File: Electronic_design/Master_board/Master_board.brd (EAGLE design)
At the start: 100 x 80 mm, 36 parts, among them IC1 74LS241N

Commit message: CRC OK
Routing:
- net VCC: track 99.8 -> 101.5 mm
- net VIN: track 51.7 -> 52.5 mm
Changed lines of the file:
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@@
 <wire x1="64.77" y1="76.2" x2="66.04" y2="76.2" width="0.508" layer="16"/>
 <wire x1="66.04" y1="76.2" x2="68.58" y2="73.66" width="0.508" layer="16"/>
-<wire x1="68.58" y1="73.66" x2="78.74" y2="73.66" width="0.508" layer="16"/>
-<wire x1="83.82" y1="78.74" x2="86.52920625" y2="78.74" width="0.508" layer="16"/>
-<wire x1="86.52920625" y1="78.74" x2="86.55460625" y2="78.7654" width="0.508" layer="16"/>
-<wire x1="95.18239375" y1="78.7654" x2="95.20779375" y2="78.74" width="0.508" layer="16"/>
-<wire x1="95.20779375" y1="78.74" x2="99.06" y2="78.74" width="0.508" layer="16"/>
-<wire x1="86.55460625" y1="78.7654" x2="95.18239375" y2="78.7654" width="0.508" layer="16"/>
-<wire x1="99.06" y1="78.74" x2="99.06" y2="71.12" width="0.508" layer="16"/>
+<wire x1="68.58" y1="73.66" x2="78.359" y2="73.66" width="0.508" layer="16"/>
+<wire x1="83.439" y1="78.994" x2="86.52920625" y2="78.994" width="0.508" layer="16"/>
+<wire x1="86.52920625" y1="78.994" x2="86.42760625" y2="79.0194" width="0.508" layer="16"/>
+<wire x1="95.56339375" y1="79.1464" x2="95.08079375" y2="79.121" width="0.508" layer="16"/>
+<wire x1="95.08079375" y1="79.121" x2="99.06" y2="79.121" width="0.508" layer="16"/>
+<wire x1="86.42760625" y1="79.0194" x2="95.56339375" y2="79.1464" width="0.508" layer="16"/>
+<wire x1="99.06" y1="79.121" x2="99.06" y2="71.12" width="0.508" layer="16"/>
 <wire x1="99.06" y1="71.12" x2="97.7618" y2="71.12" width="0.508" layer="16"/>
 <via x="97.7618" y="71.12" extent="1-16" drill="0.35"/>
-<wire x1="78.74" y1="73.66" x2="83.82" y2="78.74" width="0.508" layer="16"/>
+<wire x1="78.359" y1="73.66" x2="83.439" y2="78.994" width="0.508" layer="16"/>
 <wire x1="97.7618" y1="71.12" x2="96.4726625" y2="71.12" width="0.508" layer="1"/>
 </signal>
@@
 <wire x1="59.69" y1="76.2" x2="59.69" y2="72.39" width="2.54" layer="16"/>
 <wire x1="59.69" y1="72.39" x2="60.96" y2="71.12" width="2.54" layer="16"/>
-<wire x1="84.709" y1="77.089" x2="94.488" y2="77.089" width="2.54" layer="16"/>
-<wire x1="94.488" y1="77.089" x2="95.25" y2="76.327" width="2.54" layer="16"/>
+<wire x1="84.709" y1="77.216" x2="94.488" y2="77.216" width="2.54" layer="16"/>
+<wire x1="94.488" y1="77.216" x2="95.25" y2="76.327" width="2.54" layer="16"/>
 <wire x1="95.25" y1="76.327" x2="95.25" y2="73.66" width="2.54" layer="16"/>
 <wire x1="81.28" y1="71.12" x2="60.96" y2="71.12" width="2.54" layer="16"/>
-<wire x1="81.28" y1="71.12" x2="84.709" y2="77.089" width="2.54" layer="16"/>
+<wire x1="81.28" y1="71.12" x2="84.709" y2="77.216" width="2.54" layer="16"/>
 <wire x1="95.25" y1="73.66" x2="95.25" y2="67.31" width="2.54" layer="16"/>
 <contactref element="C3" pad="+"/>
@@
 <wire x1="15.24" y1="72.39" x2="16.51" y2="71.12" width="2.54" layer="1"/>
 <contactref element="C4" pad="+"/>
-<wire x1="16.51" y1="71.12" x2="15.748" y2="71.12" width="0" layer="19" extent="1-1"/>
+<wire x1="15.748" y1="71.12" x2="16.51" y2="71.12" width="0.1524" layer="1"/>
 </signal>
 <signal name="3V3">

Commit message: modif piste
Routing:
- net VCC: track 101.5 -> 100.5 mm
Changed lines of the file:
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@@
 <wire x1="66.04" y1="76.2" x2="68.58" y2="73.66" width="0.508" layer="16"/>
 <wire x1="68.58" y1="73.66" x2="78.359" y2="73.66" width="0.508" layer="16"/>
-<wire x1="83.439" y1="78.994" x2="86.52920625" y2="78.994" width="0.508" layer="16"/>
-<wire x1="86.52920625" y1="78.994" x2="86.42760625" y2="79.0194" width="0.508" layer="16"/>
-<wire x1="95.56339375" y1="79.1464" x2="95.08079375" y2="79.121" width="0.508" layer="16"/>
-<wire x1="95.08079375" y1="79.121" x2="99.06" y2="79.121" width="0.508" layer="16"/>
-<wire x1="86.42760625" y1="79.0194" x2="95.56339375" y2="79.1464" width="0.508" layer="16"/>
 <wire x1="99.06" y1="79.121" x2="99.06" y2="71.12" width="0.508" layer="16"/>
 <wire x1="99.06" y1="71.12" x2="97.7618" y2="71.12" width="0.508" layer="16"/>
 <via x="97.7618" y="71.12" extent="1-16" drill="0.35"/>
-<wire x1="78.359" y1="73.66" x2="83.439" y2="78.994" width="0.508" layer="16"/>
+<wire x1="78.359" y1="73.66" x2="83.42574375" y2="79.10675" width="0.508" layer="16"/>
+<wire x1="83.42574375" y1="79.10675" x2="83.439" y2="79.121" width="0.508" layer="16"/>
 <wire x1="97.7618" y1="71.12" x2="96.4726625" y2="71.12" width="0.508" layer="1"/>
+<wire x1="99.04575" y1="79.10675" x2="99.06" y2="79.121" width="0.508" layer="16"/>
+<wire x1="83.42574375" y1="79.10675" x2="99.04575" y2="79.10675" width="0.508" layer="16"/>
+<wire x1="99.04575" y1="79.10675" x2="99.06" y2="79.121" width="0.508" layer="16"/>
 </signal>
 <signal name="CTRL_AX">

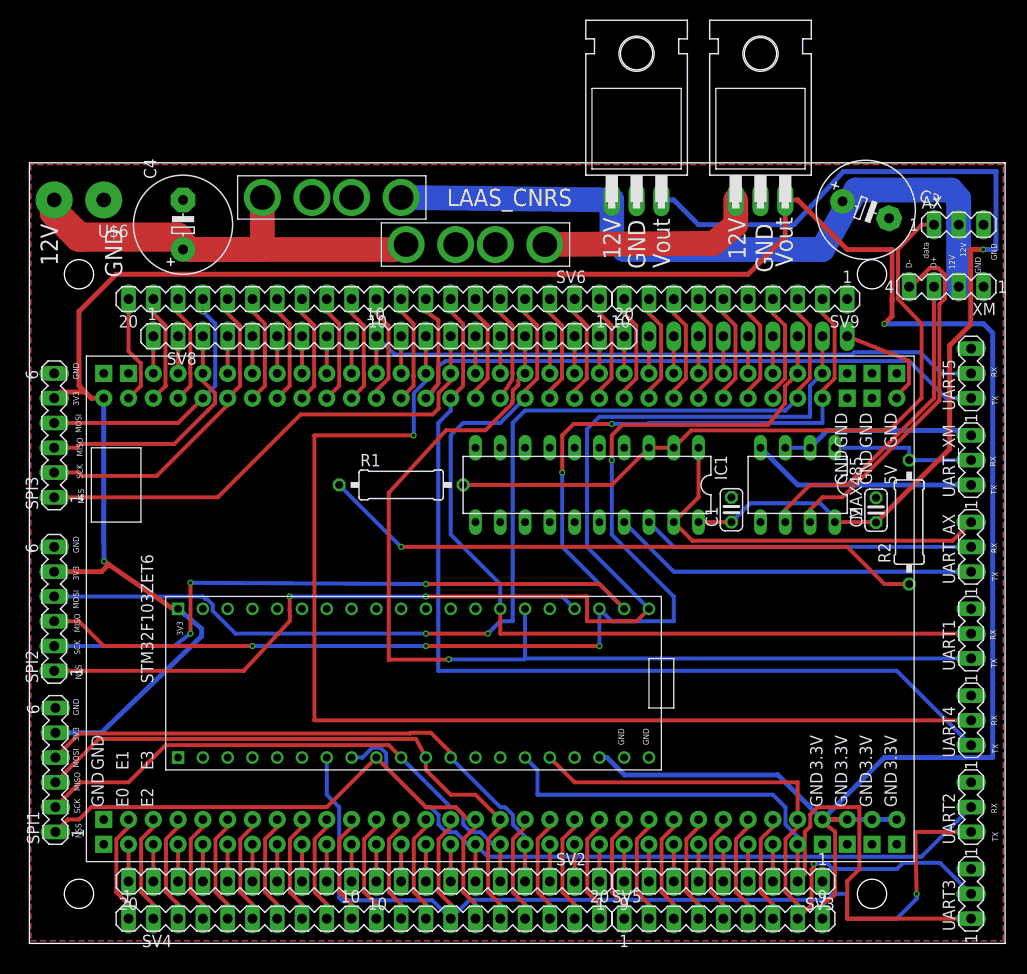
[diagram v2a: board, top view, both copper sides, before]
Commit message: ajout leds alim
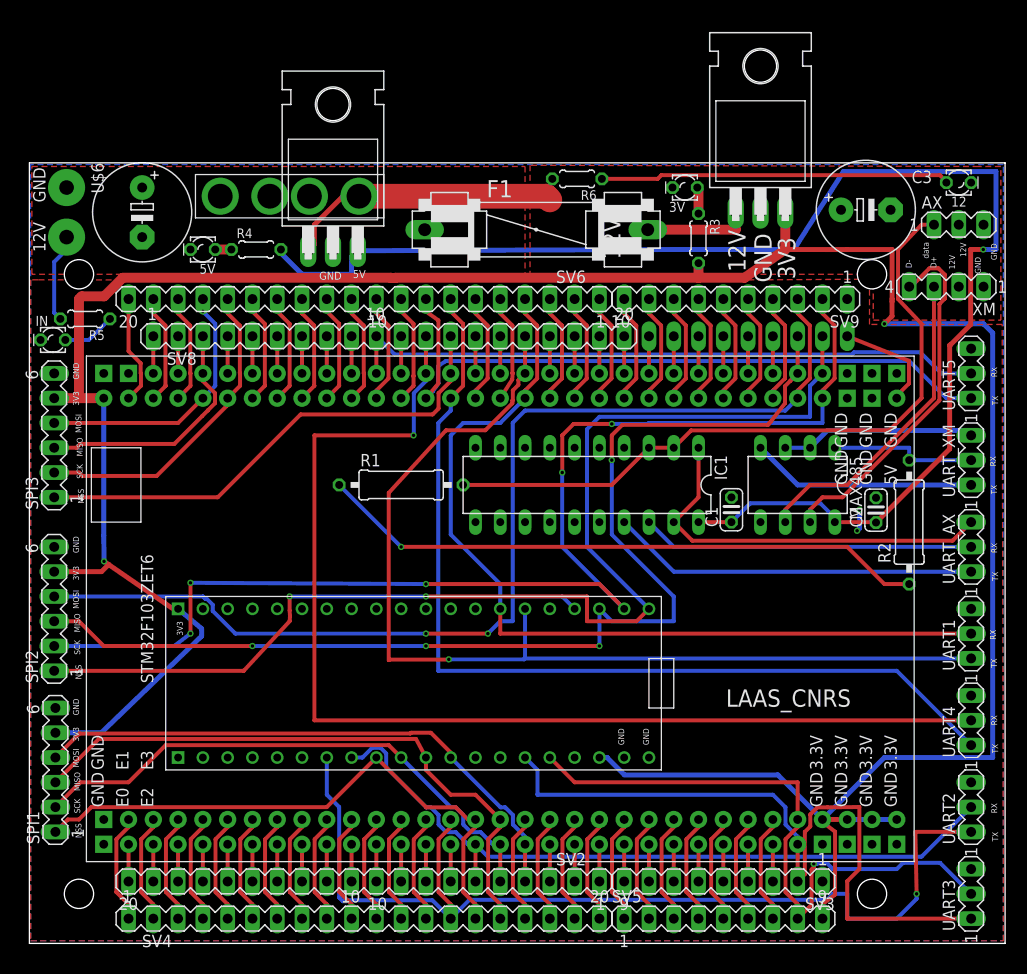
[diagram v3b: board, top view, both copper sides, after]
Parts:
- removed U$3: AUTO_FUSE, AUTO_FUSE:AUTO_FUSE
- added 12, 3V, 5V, IN: (no value), eagle-ltspice:LED_LD260
- added F1: (no value), special:FUSE
- added R3, R4, R5, R6: (no value), resistor:0204/5
- moved 5V_AX 31.5 mm to (31.1, 81.2)
- moved C4 4.38 mm to (11.6, 74.9), turned to 270 degrees
- moved U$4 4.32 mm to (26.7, 76.6)
- moved U$6 1.80 mm to (3.81, 74.9), turned to 270 degrees
- moved 3V3 1.27 mm to (74.9, 85.1)
- turned C3 to 0 degrees
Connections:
- new net N$1: 3V.A, R3.1
- new net N$2: 5V.A, R4.1
- new net N$3: IN.A, R5.1
- new net N$4: 12.A, R6.1
- net 12V: now also R6.2
- net 3V3: now also R3.2
- net GND: now also 12.K, 3V.K, 5V.K, IN.K
- net N$121: now also F1.2; no longer U$3.P$4
- net VCC: now also R4.2
- net VIN: now also F1.1, R5.2; no longer U$3.P$2
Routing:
- net 12V: track 79.8 -> 28.4 mm
- net VIN: track 52.5 -> 9.17 mm
- net VCC: track 100.5 -> 143.7 mm
- net N$4: track 0.00 -> 35.8 mm
- net N$121: track 22.8 -> 10.8 mm
- net N$3: track 0.00 -> 5.47 mm
- net N$1: track 0.00 -> 2.72 mm
- net GND: track 0.00 -> 2.26 mm, vias 0 -> 2
- net N$2: track 0.00 -> 1.65 mm
- net 3V3: track 288.9 -> 288.0 mm
- added copper zone on layer 1, net 12V
- added copper zone on layer 1, net VIN
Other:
- board text added: "5V"
- board text removed: "Vout"
